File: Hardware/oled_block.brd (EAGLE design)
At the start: 30.5 x 44.5 mm, 35 parts, among them J1 EDISON_CONNECTOR_FULLMOUNTING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

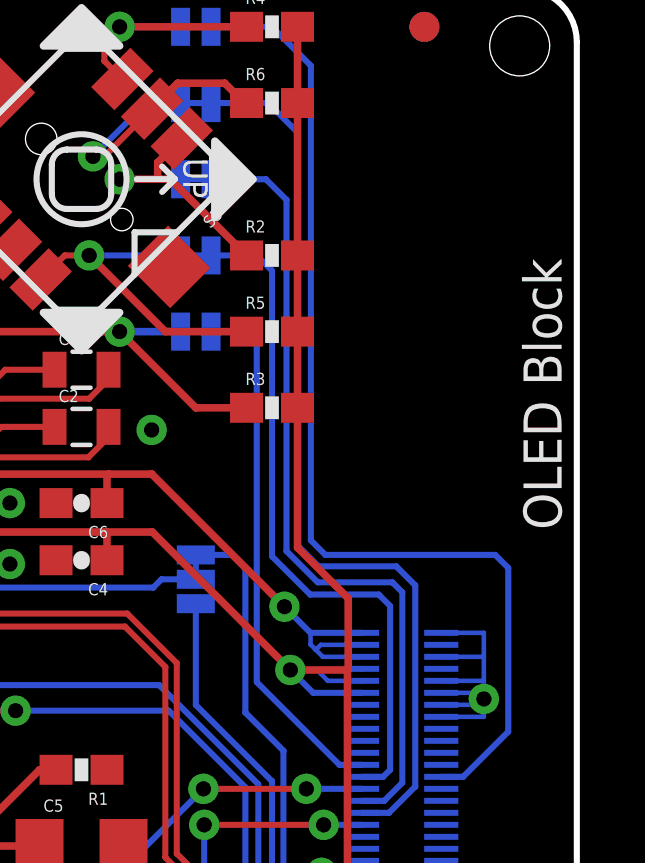
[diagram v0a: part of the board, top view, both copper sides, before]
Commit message: adjusting a few traces
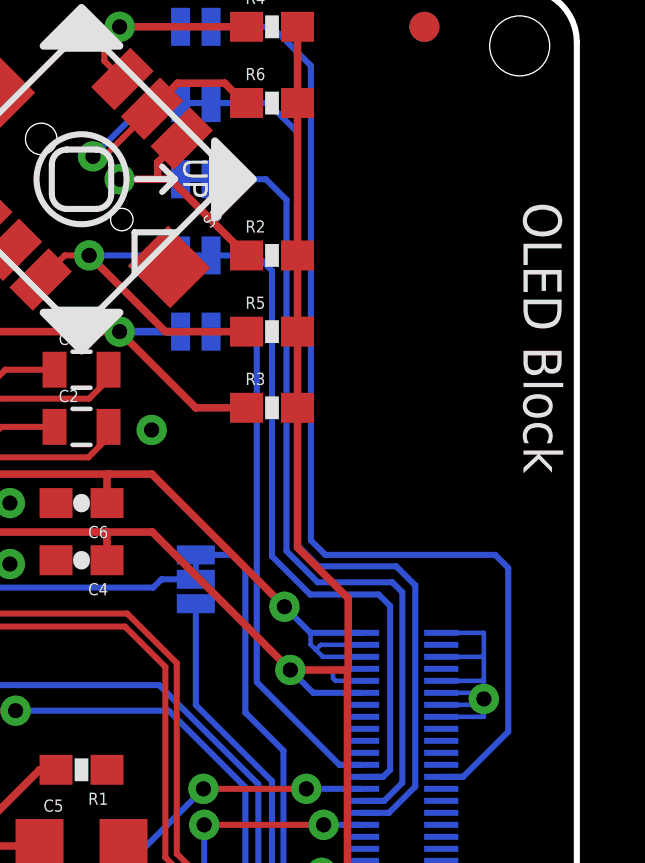
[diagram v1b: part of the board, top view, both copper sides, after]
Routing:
- net 3.3V: track 3.12 -> 2.25 mm
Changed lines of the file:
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@@
 <grid distance="0.025" unitdist="inch" unit="inch" style="lines" multiple="1" display="yes" altdistance="0.005" altunitdist="inch" altunit="inch"/>
 <layers>
-<layer number="1" name="Top" color="4" fill="1" visible="yes" active="yes"/>
+<layer number="1" name="Top" color="4" fill="1" visible="no" active="yes"/>
 <layer number="2" name="Route2" color="1" fill="3" visible="no" active="no"/>
 <layer number="3" name="Route3" color="4" fill="3" visible="no" active="no"/>
@@
 <layer number="19" name="Unrouted" color="6" fill="1" visible="yes" active="yes"/>
 <layer number="20" name="Dimension" color="15" fill="1" visible="yes" active="yes"/>
-<layer number="21" name="tPlace" color="16" fill="1" visible="yes" active="yes"/>
+<layer number="21" name="tPlace" color="16" fill="1" visible="no" active="yes"/>
 <layer number="22" name="bPlace" color="14" fill="1" visible="yes" active="yes"/>
 <layer number="23" name="tOrigins" color="15" fill="1" visible="yes" active="yes"/>
@@
 <layer number="49" name="Reference" color="7" fill="1" visible="no" active="yes"/>
 <layer number="50" name="dxf" color="7" fill="1" visible="no" active="no"/>
-<layer number="51" name="tDocu" color="6" fill="1" visible="yes" active="yes"/>
-<layer number="52" name="bDocu" color="7" fill="1" visible="no" active="yes"/>
+<layer number="51" name="tDocu" color="6" fill="1" visible="no" active="yes"/>
+<layer number="52" name="bDocu" color="7" fill="1" visible="yes" active="yes"/>
 <layer number="53" name="tGND_GNDA" color="7" fill="9" visible="no" active="no"/>
 <layer number="54" name="bGND_GNDA" color="1" fill="9" visible="no" active="no"/>
@@
 <text x="19.05" y="2.286" size="1.27" layer="21" font="vector" ratio="15" rot="SR270" align="center">A</text>
 <text x="7.62" y="2.286" size="1.27" layer="21" font="vector" ratio="15" rot="SR270" align="center">B</text>
-<text x="29.972" y="26.416" size="1.27" layer="21" font="vector" ratio="15" rot="SR90">OLED Block</text>
+<text x="28.702" y="37.338" size="1.27" layer="21" font="vector" ratio="15" rot="SR270">OLED Block</text>
 <text x="16.51" y="43.18" size="0.889" layer="22" font="vector" ratio="15" rot="MR180" align="center-right">L</text>
 <text x="16.51" y="40.64" size="0.889" layer="22" font="vector" ratio="15" rot="MR180" align="center-right">C</text>
@@
 <signals>
 <signal name="GND">
-<polygon width="0.1778" layer="16" spacing="0.254" isolate="0.1524" orphans="yes" rank="6">
+<polygon width="0.1778" layer="16" spacing="0.254" isolate="0.1524" rank="6">
 <vertex x="30.48" y="42.672"/>
 <vertex x="30.48" y="1.778" curve="-90"/>
@@
 <vertex x="28.702" y="44.45" curve="-90"/>
 </polygon>
-<polygon width="0.1778" layer="1" spacing="0.254" isolate="0.1524" orphans="yes" rank="6">
+<polygon width="0.1778" layer="1" spacing="0.254" isolate="0.1524" rank="6">
 <vertex x="30.48" y="1.728" curve="-90"/>
 <vertex x="28.752" y="0"/>
@@
 <contactref element="J1" pad="8"/>
 <contactref element="J1" pad="10"/>
-<wire x1="23.32" y1="21.38" x2="22.181" y2="21.38" width="0.1524" layer="16"/>
-<wire x1="22.181" y1="21.38" x2="21.844" y2="21.717" width="0.1524" layer="16"/>
-<wire x1="23.32" y1="21.78" x2="21.907" y2="21.78" width="0.1524" layer="16"/>
-<wire x1="21.907" y1="21.78" x2="21.844" y2="21.717" width="0.1524" layer="16"/>
+<wire x1="23.32" y1="21.38" x2="22.435" y2="21.38" width="0.1524" layer="16"/>
+<wire x1="23.32" y1="21.78" x2="22.415" y2="21.78" width="0.1524" layer="16"/>
+<wire x1="22.435" y1="21.38" x2="22.352" y2="21.463" width="0.1524" layer="16"/>
+<wire x1="22.415" y1="21.78" x2="22.352" y2="21.717" width="0.1524" layer="16"/>
+<wire x1="22.352" y1="21.717" x2="22.352" y2="21.463" width="0.1524" layer="16"/>
 </signal>
 <signal name="GP183_PWM3">

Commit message: Ready for reds Added VSYS header No known to-do items
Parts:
- added JP1: M02PTH, SparkFun-Connectors:1X02
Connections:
- net GND: now also JP1.1
- net VSYS: now also JP1.2
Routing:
- net VSYS: track 21.7 -> 33.6 mm
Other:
- board text added: "+"
- board text added: "-"
- board text added: "3.3-4.2V"
